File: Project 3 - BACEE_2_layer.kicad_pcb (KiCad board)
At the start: 2 copper layers, 40.4 x 29.7 mm, 17 parts, among them J1 Digital pins, J2 Serial, J3 ICSP, J4 I2C, U1 DS1337S, U2 24LC1025, U3 24LC1025, U4 ATMEGA328P-AU, Y1 Crystal 32 MHz, Y2 Crystal 16 MHz

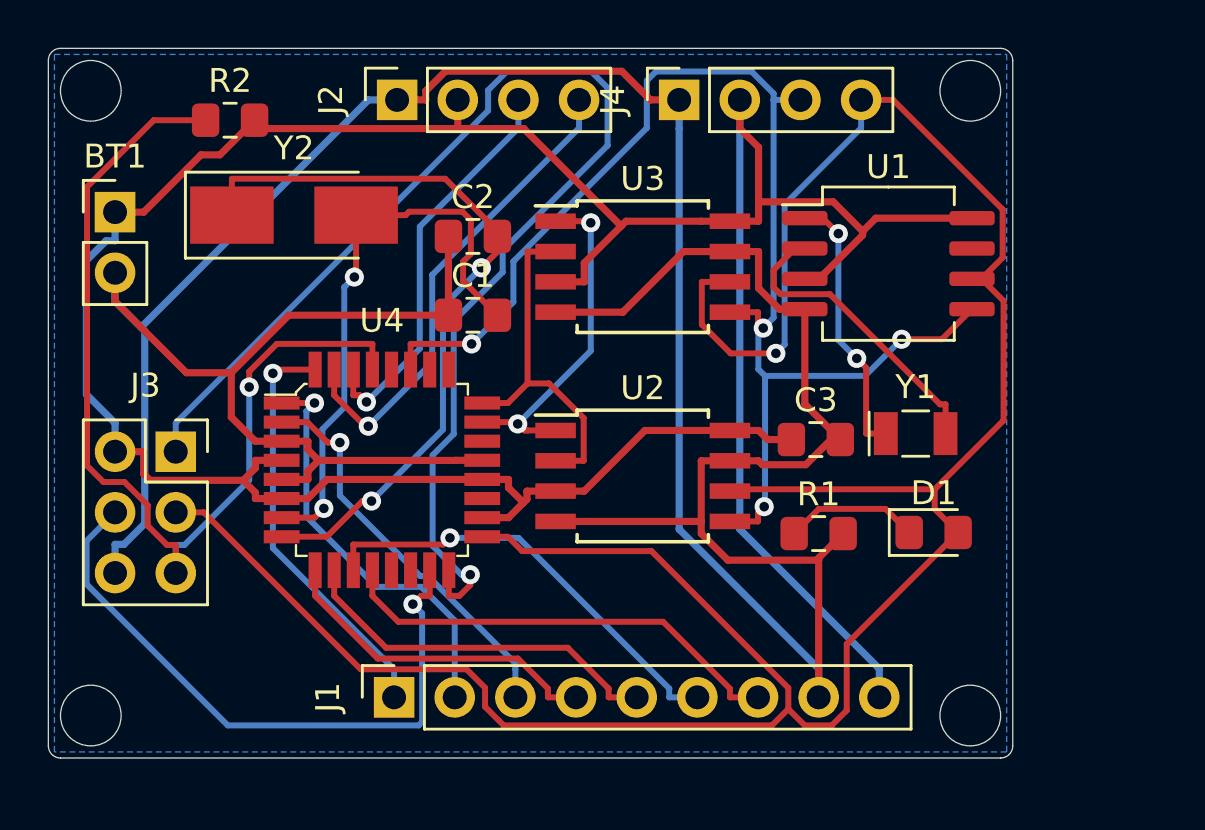
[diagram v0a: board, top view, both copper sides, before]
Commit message: Completed work in silkscreen layers.
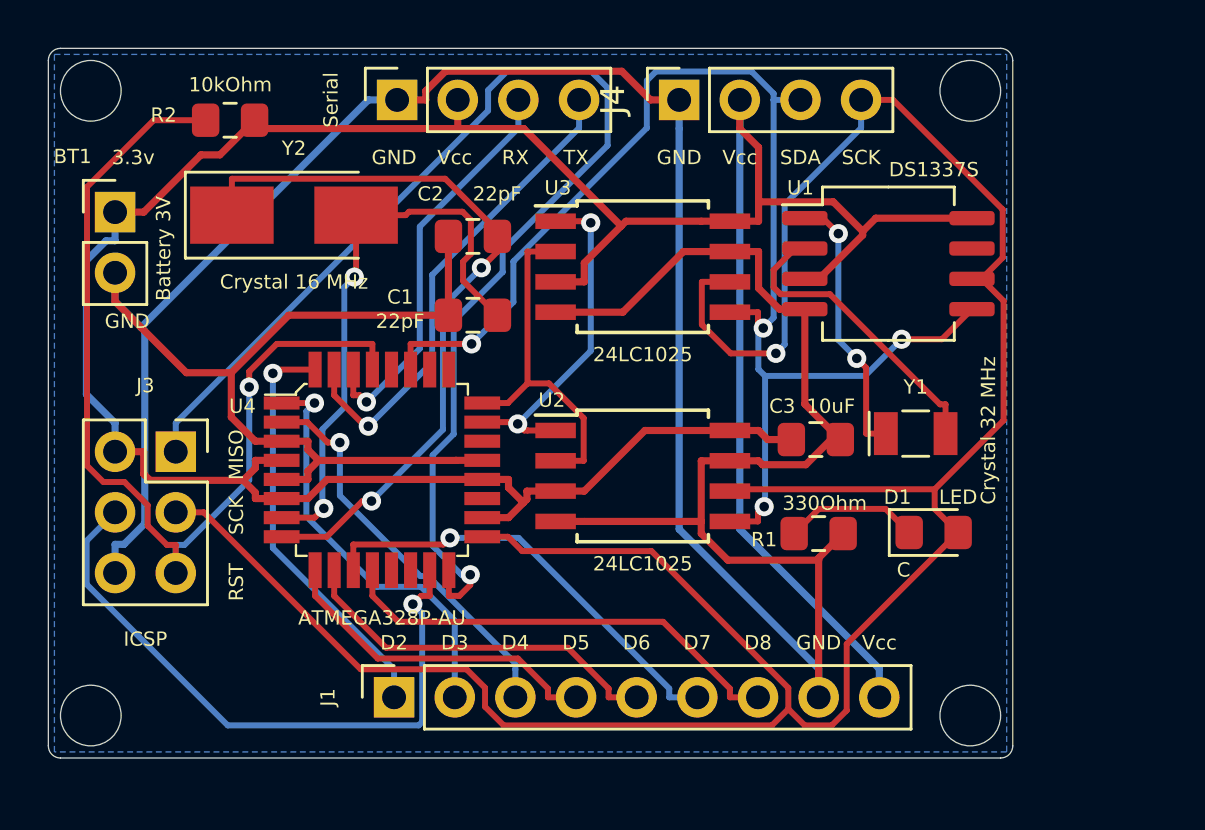
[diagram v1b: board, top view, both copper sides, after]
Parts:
- added REF**: OSHW-Logo2_9.8x8mm_SilkScreen, Symbol:OSHW-Logo2_9.8x8mm_SilkScreen, B.Cu at (77.0, 101.1)
- added REF**: KiCad-Logo_6mm_SilkScreen, Symbol:KiCad-Logo_6mm_SilkScreen, B.Cu at (87.6, 104.4)
- renumbered J2 to Serial
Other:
- board text added: "3.3v"
- board text added: "Arduino clone with: - 2 Mbit EEPROM - Clock & calendar - I2C, SPI, GPIO"
- board text added: "Battery 3V"
- board text added: "C"
- board text added: "D2"
- board text added: "D3"
- board text added: "D4"
- board text added: "D5"
- board text added: "D6"
- board text added: "D7"
- board text added: "D8"
- board text added: "Designed by Emmanuel"
- board text added: "GND"
- board text added: "MISO"
- board text added: "RST"
- board text added: "RX"
- board text added: "SCK"
- board text added: "SDA"
- board text added: "TX"
- board text added: "Vcc"

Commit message: Added the gerber files.
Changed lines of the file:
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@@
     (pcbplotparams
       (layerselection 0x010fc_ffffffff)
-      (usegerberextensions false)
+      (usegerberextensions true)
       (usegerberattributes true)
       (usegerberadvancedattributes true)
@@
       (outputformat 1)
       (mirror false)
-      (drillshape 1)
+      (drillshape 0)
       (scaleselection 1)
-      (outputdirectory ""))
+      (outputdirectory "BACEE-Gerbers/"))
   )
   (net 0 "")
@@
     (descr "Through hole straight socket strip, 1x04, 2.54mm pitch, single row (from Kicad 4.0.7), script generated")
     (tags "Through hole socket strip THT 1x04 2.54mm single row")
-    (fp_text reference J4 (at 0 -2.77 90) (layer F.SilkS)
-      (effects (font (size 1 1) (thickness 0.15)))
+    (fp_text reference J4 (at -0.127 -2.286 90) (layer F.SilkS)
+      (effects (font (size 0.6 0.6) (thickness 0.15)))
     )
     (fp_text value I2C (at 0 10.39 90) (layer F.Fab)
@@
     (polygon
       (pts
-        (xy 91.948 118.364) (xy 52.07 118.364) (xy 52.07 89.154) (xy 91.948 89.154)
+        (xy 98.244993 119.634) (xy 58.366993 119.634) (xy 58.366993 90.424) (xy 98.244993 90.424)
       )
     )
